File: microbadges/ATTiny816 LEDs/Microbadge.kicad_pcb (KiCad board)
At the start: 2 copper layers, 6 x 6 mm, 13 parts, among them U1 ATtiny816-M

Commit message: Update to Bit-banged I2C
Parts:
- MCB1: footprint Microbadge V2:Microbadge_V2_simple_round -> Microbadge V2:Microbadge_V2_full_round
- moved R1 2.38 mm to (147.8, 101.7)
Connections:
- R1 pad 1: +VBATT -> UPDI_PROG
- R1 pad 2: UPDI_PROG -> +VBATT
- U1 pad 15: unconnected-(U1-PC0-Pad15) -> SDA
- U1 pad 16: unconnected-(U1-PC1-Pad16) -> SCL
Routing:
- net SDA: track 0.00 -> 1.21 mm
- net SCL: track 0.00 -> 1.17 mm
- net UPDI_PROG: track 3.15 -> 2.15 mm

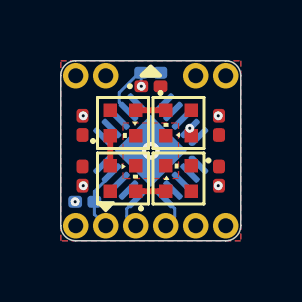
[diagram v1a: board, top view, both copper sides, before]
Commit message: Update I2C pins
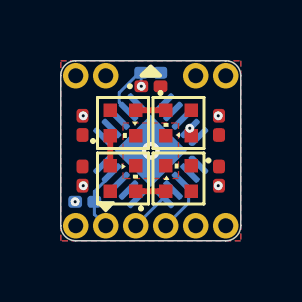
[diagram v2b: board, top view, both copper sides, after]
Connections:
- U1 pad 13: unconnected-(U1-PB1-Pad13) -> SDA
- U1 pad 14: unconnected-(U1-PB0-Pad14) -> SCL
- U1 pad 15: SDA -> SCL
- U1 pad 16: SCL -> unconnected-(U1-PC1-Pad16)
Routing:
- net SDA: track 1.21 -> 1.92 mm
- net SCL: track 1.17 -> 1.74 mm
